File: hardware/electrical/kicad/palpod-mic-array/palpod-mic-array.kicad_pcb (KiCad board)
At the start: 4 copper layers, 120 x 120 mm, 0 parts

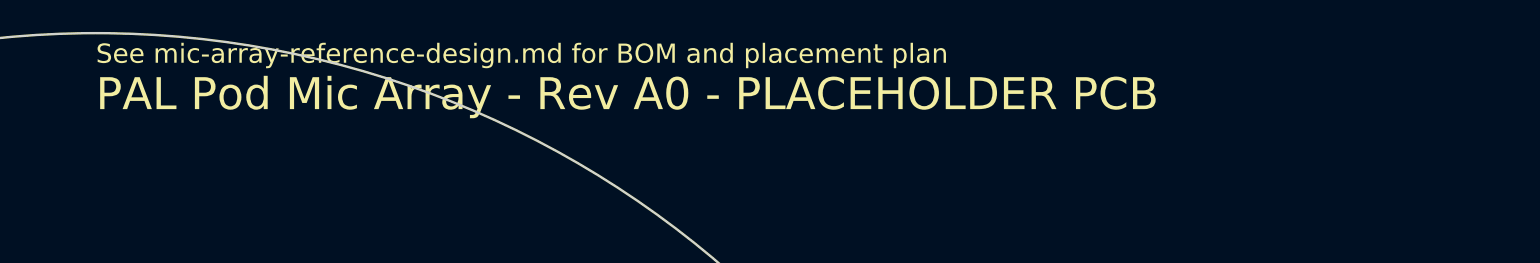
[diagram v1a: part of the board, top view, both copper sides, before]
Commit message: brand: broad KiCad sweep — remaining PAL Pod strings → Hearth
Targeted-pattern sed in ff14a48 missed variants. Broad find-replace
on .kicad_sch/pcb/pro/sym/mod + fp-lib-table + sym-lib-table +
per-project README.md (only where PAL Pod string actually appeared).
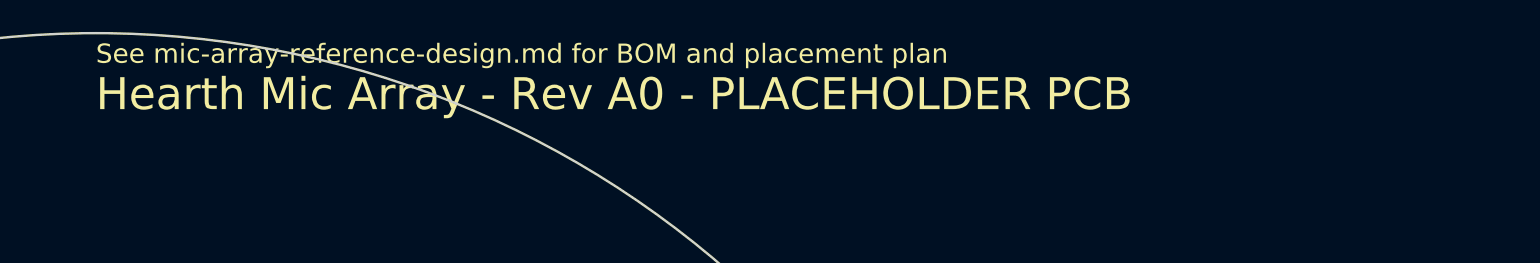
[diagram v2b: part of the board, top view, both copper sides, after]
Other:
- board text added: "Hearth Mic Array - Rev A0 - PLACEHOLDER PCB"
- board text removed: "PAL Pod Mic Array - Rev A0 - PLACEHOLDER PCB"
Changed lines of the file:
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@@
   (paper "A3")
   (title_block
-    (title "PAL Pod Mic Array - PCB")
+    (title "Hearth Mic Array - PCB")
     (date "2026-08-03")
     (rev "A0")
@@
     (uuid "d3af5a92-3b41-4b32-8b6f-ab00000edge1")
   )
-  (gr_text "PAL Pod Mic Array - Rev A0 - PLACEHOLDER PCB"
+  (gr_text "Hearth Mic Array - Rev A0 - PLACEHOLDER PCB"
     (at 0 -55 0)
     (layer "F.SilkS")
